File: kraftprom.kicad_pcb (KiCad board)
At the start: 2 copper layers, 67.5 x 82.6 mm, 21 parts, among them J1 Jumper_3_Bridged12, J2 PROGRAM, U1 PIC16F628A, U2 74HC164, U3 74HC164, U4 74HC164, U5 74LS245, U6 74LS165, U7 FTDI USB ADAPTER

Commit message: More PCB design.
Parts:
- moved G*** 0.91 mm to (141.7, 60.2)
- moved J1 0.20 mm to (139.6, 78.5)
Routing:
- net Earth: track 349.0 -> 330.6 mm, vias 8 -> 6
- net Net-(U1-RB2/TX/CK): track 64.9 -> 50.9 mm, vias 3 -> 1
- net Net-(U5-B2): track 62.3 -> 49.6 mm, vias 3 -> 1
- net Net-(U3-Q0): track 51.1 -> 43.3 mm, vias 3 -> 1
- net Net-(U1-RA3/AN3/CMP1): track 49.1 -> 42.0 mm, vias 1 -> 0
- net Net-(U3-Q7): track 51.4 -> 44.4 mm
- net Net-(U2-Q1): track 51.3 -> 44.7 mm
- net Net-(U1-RB1/RX/DT): track 63.9 -> 58.3 mm, vias 3 -> 0
- net Net-(J1-C): track 40.1 -> 34.9 mm
- net Net-(U2-Q5): track 73.2 -> 68.2 mm
- net Net-(U2-Q7): track 53.6 -> 48.6 mm, vias 3 -> 2
- net Net-(U2-Q2): track 46.6 -> 41.8 mm
- net Net-(U2-Q0): track 52.9 -> 48.5 mm
- net Net-(U2-Q6): track 32.0 -> 28.6 mm, vias 3 -> 2
- net Net-(U4-Q0): track 23.6 -> 20.4 mm, vias 2 -> 1
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
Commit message: More PCB design.
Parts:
- moved C6 1.91 mm to (100.4, 112.2)
- moved U6 1.77 mm to (92.8, 115.6)
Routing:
- net Earth: track 330.6 -> 327.8 mm, vias 6 -> 8
- net Net-(U5-B1): track 63.3 -> 61.0 mm
- net +5V: track 222.7 -> 220.8 mm, vias 1 -> 0
- net /~{VERLOAD}: track 21.3 -> 19.5 mm
- net Net-(U5-B0): track 55.3 -> 57.0 mm
- net Net-(U5-B7): track 75.5 -> 77.2 mm
- net /VERREAD: track 54.8 -> 53.2 mm
- net Net-(U5-B4): track 60.9 -> 62.3 mm
- net /VERCLK: track 16.5 -> 15.2 mm
- net Net-(U5-B6): track 71.8 -> 73.1 mm
- net Net-(U5-B5): track 65.9 -> 67.1 mm
- net Net-(U5-B3): track 58.0 -> 57.1 mm
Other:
- board size 67.5 x 82.6 mm -> 67.5 x 85.8 mm
- board text added: "Rev 1.0 ©2025 ARMCoder"
- board text removed: "Rev 1.0 ARMCoder"

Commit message: More PCB design (fixes).
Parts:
- moved J1 5.19 mm to (144.4, 80.3), turned to -90 degrees
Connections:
- U7 pad 12: Net-(U1-RA3/AN3/CMP1) -> unconnected-(U7-~{RTS}-Pad12)
- U7 pad 4: unconnected-(U7-~{CTS}-Pad4) -> Net-(U1-RA3/AN3/CMP1)
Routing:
- net Net-(U1-RA3/AN3/CMP1): track 42.0 -> 29.6 mm, vias 0 -> 1
- net /~{WE}: track 99.7 -> 94.6 mm
- net Net-(J1-B): track 39.2 -> 42.5 mm

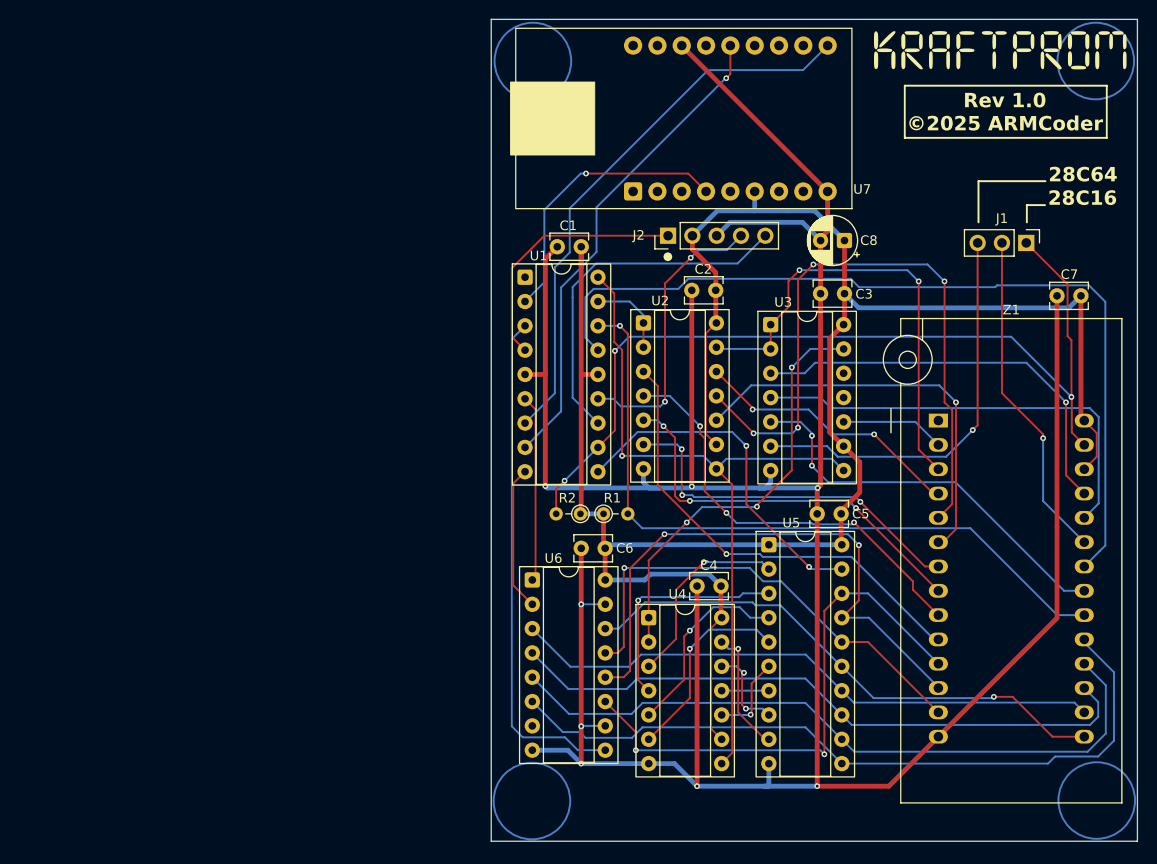
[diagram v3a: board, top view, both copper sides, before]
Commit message: More PCB design (clearances).
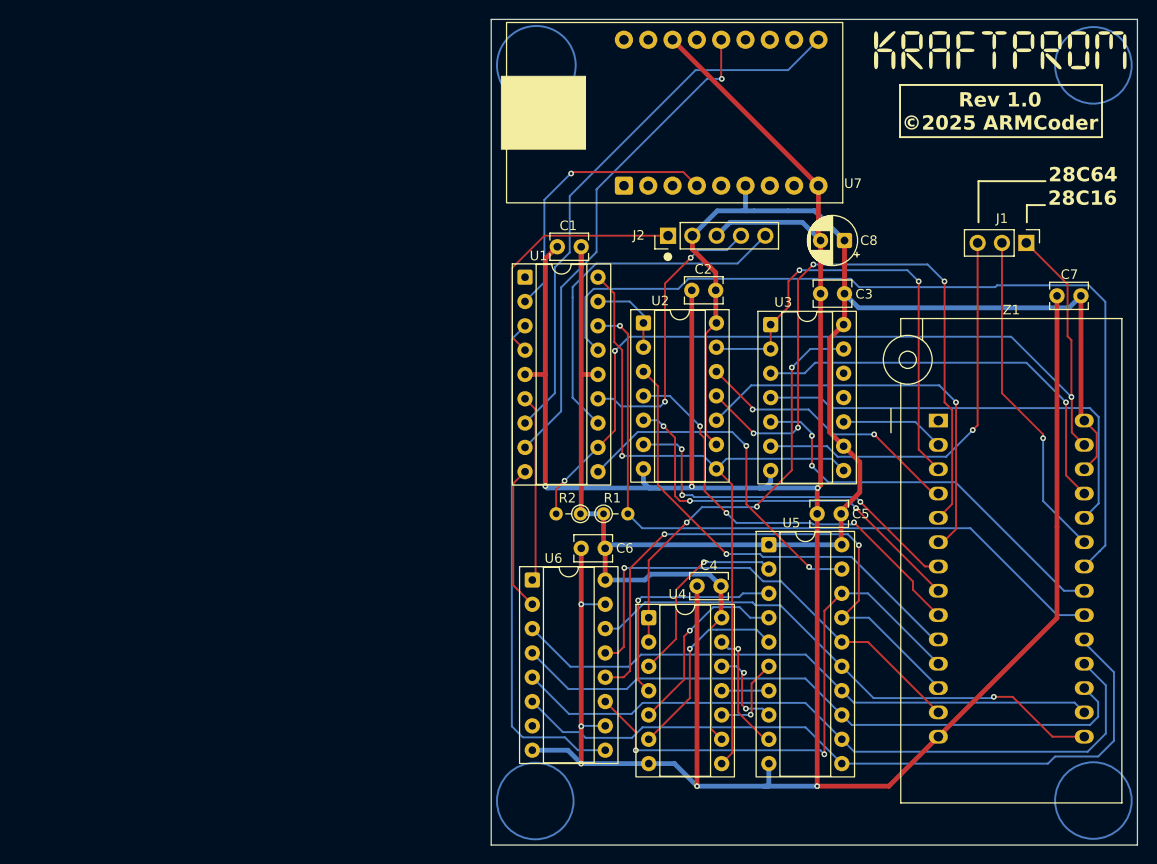
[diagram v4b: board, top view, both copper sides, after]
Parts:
- moved U7 1.13 mm to (104.9, 66.8)
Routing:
- net Net-(U1-RB2/TX/CK): track 50.9 -> 52.0 mm
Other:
- board size 67.5 x 85.8 mm -> 67.5 x 86.2 mm
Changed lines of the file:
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@@
 	(footprint "Kraft80:FTDI-ADAPTER"
 		(layer "F.Cu")
-		(at 105.86 67.355 180)
+		(at 104.9 66.75 180)
 		(property "Reference" "U7"
 			(at -21.39 -7.395 0)
@@
 	)
 	(gr_circle
-		(center 92.85 61.35)
-		(end 96.85 61.35)
+		(center 93.211265 61.8)
+		(end 97.211265 60.85)
 		(stroke
 			(width 0.2)
@@
 	)
 	(gr_circle
-		(center 151.75 138.6)
-		(end 155.75 138.6)
+		(center 151.4 138.6)
+		(end 155.4 138.6)
 		(stroke
 			(width 0.2)
@@
 	)
 	(gr_circle
-		(center 151.65 61.35)
-		(end 155.65 61.35)
+		(center 151.4 61.8)
+		(end 155.4 61.8)
 		(stroke
 			(width 0.2)
@@
 	)
 	(gr_circle
-		(center 92.75 138.65)
-		(end 96.75 138.65)
+		(center 93.1 138.65)
+		(end 97.1 138.65)
 		(stroke
 			(width 0.2)
@@
 	)
 	(gr_rect
-		(start 131.7 63.925)
-		(end 152.8 69.375)
+		(start 131.2 63.85)
+		(end 152.3 69.3)
 		(stroke
 			(width 0.2)
@@
 	(gr_rect
 		(start 88.5 57)
-		(end 156 142.85)
+		(end 156 143.25)
 		(stroke
 			(width 0.05)
@@
 	)
 	(gr_text "Rev 1.0\n©2025 ARMCoder"
-		(at 142.15 68.775 0)
+		(at 141.65 68.7 0)
 		(layer "F.SilkS")
 		(effects
@@
 	)
 	(segment
+		(start 122.68 79.63)
+		(end 122.68 74.37)
+		(width 0.5)
+		(layer "F.Cu")
+		(net 3)
+	)
+	(segment
+		(start 122.9 80.1)
+		(end 122.9 79.85)
+		(width 0.5)
+		(layer "F.Cu")
+		(net 3)
+	)
+	(segment
 		(start 147.6 119.5375)
 		(end 135.2075 131.93)
@@
 	)
 	(segment
-		(start 122.9 80.1)
-		(end 122.9 79.85)
-		(width 0.5)
-		(layer "F.Cu")
-		(net 3)
-	)
-	(segment
 		(start 147.6 110)
 		(end 147.6 119.5375)
@@
 	)
 	(segment
-		(start 123.64 79.11)
-		(end 123.64 74.975)
-		(width 0.5)
-		(layer "F.Cu")
-		(net 3)
-	)
-	(segment
 		(start 122.55 106)
 		(end 122.6 105.95)
@@
 	)
 	(segment
-		(start 123.625 74.975)
-		(end 123.64 74.975)
-		(width 0.5)
-		(layer "F.Cu")
-		(net 3)
-	)
-	(segment
-		(start 108.4 59.75)
-		(end 123.625 74.975)
+		(start 122.68 74.37)
+		(end 107.44 59.13)
 		(width 0.5)
 		(layer "F.Cu")
@@
 	)
 	(segment
-		(start 122.9 79.85)
-		(end 123.64 79.11)
-		(width 0.5)
-		(layer "F.Cu")
-		(net 3)
-	)
-	(segment
 		(start 97.95 130.8)
 		(end 97.9 130.85)
@@
 	)
 	(segment
-		(start 108.4 59.735)
-		(end 108.4 59.75)
-		(width 0.5)
-		(layer "F.Cu")
-		(net 3)
-	)
-	(segment
 		(start 109.45 85.3)
 		(end 109.45 105.8)
@@
 	)
 	(segment
+		(start 122.9 79.85)
+		(end 122.68 79.63)
+		(width 0.5)
+		(layer "F.Cu")
+		(net 3)
+	)
+	(segment
 		(start 97.9 118.1)
 		(end 97.9 130.85)
@@
 	)
 	(segment
-		(start 116.02 74.975)
-		(end 116.02 76.93)
-		(width 0.5)
-		(layer "B.Cu")
-		(net 21)
-	)
-	(segment
 		(start 117.5 111.88)
 		(end 100.77 111.88)
@@
 	(segment
 		(start 114.75 77)
-		(end 115.95 77)
-		(width 0.5)
-		(layer "B.Cu")
-		(net 21)
-	)
-	(segment
-		(start 116.35 75.305)
-		(end 116.02 74.975)
+		(end 115.1 77)
 		(width 0.5)
 		(layer "B.Cu")
@@
 	)
 	(segment
-		(start 116.02 76.93)
+		(start 115.1 77)
 		(end 115.95 77)
 		(width 0.5)
@@
 	)
 	(segment
+		(start 115.1 77)
+		(end 115.06 76.96)
+		(width 0.5)
+		(layer "B.Cu")
+		(net 21)
+	)
+	(segment
 		(start 150.1 85.88)
 		(end 148.849 87.131)
@@
 	)
 	(segment
+		(start 115.06 76.96)
+		(end 115.06 74.37)
+		(width 0.5)
+		(layer "B.Cu")
+		(net 21)
+	)
+	(segment
 		(start 100.77 111.88)
 		(end 100.4 112.25)
@@
 	)
 	(segment
-		(start 92.03 99.17)
-		(end 95.15 96.05)
+		(start 109.85 62.3)
+		(end 96.7 75.45)
 		(width 0.2)
 		(layer "B.Cu")
@@
 	(segment
 		(start 95.15 96.05)
-		(end 95.15 82.9)
+		(end 92.03 99.17)
 		(width 0.2)
 		(layer "B.Cu")
@@
 	)
 	(segment
-		(start 96.7 76.74358)
-		(end 111.14358 62.3)
+		(start 96.7 81.35)
+		(end 95.15 82.9)
 		(width 0.2)
 		(layer "B.Cu")
@@
 	)
 	(segment
-		(start 121.075 62.3)
-		(end 123.64 59.735)
+		(start 122.68 59.13)
+		(end 119.51 62.3)
 		(width 0.2)
 		(layer "B.Cu")
@@
 	)
 	(segment
-		(start 111.14358 62.3)
-		(end 121.075 62.3)
+		(start 95.15 82.9)
+		(end 95.15 96.05)
 		(width 0.2)
 		(layer "B.Cu")
@@
 	)
 	(segment
-		(start 95.15 82.9)
-		(end 96.7 81.35)
+		(start 119.51 62.3)
+		(end 109.85 62.3)
 		(width 0.2)
 		(layer "B.Cu")
@@
 	)
 	(segment
-		(start 96.7 81.35)
-		(end 96.7 76.74358)
+		(start 96.7 75.45)
+		(end 96.7 81.35)
 		(width 0.2)
 		(layer "B.Cu")
@@
 	)
 	(segment
-		(start 113.05 63.15)
-		(end 113.48 62.72)
+		(start 112.585331 63.214669)
+		(end 112.52 63.149338)
 		(width 0.2)
 		(layer "F.Cu")
@@
 	)
 	(segment
-		(start 113.48 62.72)
-		(end 113.48 59.735)
+		(start 112.52 63.149338)
+		(end 112.52 59.13)
 		(width 0.2)
 		(layer "F.Cu")
@@
 	)
 	(via
-		(at 113.05 63.15)
+		(at 112.585331 63.214669)
 		(size 0.6)
 		(drill 0.3)
@@
 	)
 	(segment
-		(start 113.05 63.15)
-		(end 112.98171 63.15)
+		(start 95.8 97.94)
+		(end 92.03 101.71)
 		(width 0.2)
 		(layer "B.Cu")
@@
 	)
 	(segment
-		(start 99.5 81.3)
-		(end 95.8 85)
+		(start 99.5 74.75)
+		(end 99.5 81.3)
 		(width 0.2)
 		(layer "B.Cu")
@@
 	)
 	(segment
-		(start 95.8 97.94)
-		(end 92.03 101.71)
+		(start 95.8 85)
+		(end 95.8 97.94)
 		(width 0.2)
 		(layer "B.Cu")
@@
 	)
 	(segment
-		(start 112.98171 63.15)
-		(end 99.5 76.63171)
+		(start 99.5 81.3)
+		(end 95.8 85)
 		(width 0.2)
 		(layer "B.Cu")
@@
 	)
 	(segment
-		(start 99.5 76.63171)
-		(end 99.5 81.3)
+		(start 99.5 74.75)
+		(end 111.035331 63.214669)
 		(width 0.2)
 		(layer "B.Cu")
@@
 	)
 	(segment
-		(start 95.8 85)
-		(end 95.8 97.94)
+		(start 111.035331 63.214669)
+		(end 112.585331 63.214669)
 		(width 0.2)
 		(layer "B.Cu")
@@
 	)
 	(segment
-		(start 109.065 73.1)
-		(end 110.94 74.975)
+		(start 97 72.95)
+		(end 108.56 72.95)
+		(width 0.2)
+		(layer "F.Cu")
+		(net 60)
+	)
+	(segment
+		(start 96.85 73.1)
+		(end 97 72.95)
 		(width 0.2)
 		(layer "F.Cu")
@@
 	)
 	(segment
-		(start 98.4 73.1)
-		(end 109.065 73.1)
+		(start 108.56 72.95)
+		(end 109.98 74.37)
 		(width 0.2)
 		(layer "F.Cu")
@@
 	)
 	(via
-		(at 98.4 73.1)
+		(at 96.85 73.1)
 		(size 0.6)
 		(drill 0.3)
@@
 	)
 	(segment
-		(start 94.05 76.9)
-		(end 97.85 73.1)
+		(start 94.05 84.45)
+		(end 92.03 86.47)
 		(width 0.2)
 		(layer "B.Cu")
@@
 	)
 	(segment
-		(start 97.85 73.1)
-		(end 98.4 73.1)
+		(start 96.8 73.1)
+		(end 94.05 75.85)
 		(width 0.2)
 		(layer "B.Cu")
@@
 	)
 	(segment
-		(start 92.03 86.47)
+		(start 94.05 75.85)
 		(end 94.05 84.45)
 		(width 0.2)
@@
 	)
 	(segment
-		(start 94.05 84.45)
-		(end 94.05 76.9)
+		(start 96.85 73.1)
+		(end 96.8 73.1)
 		(width 0.2)
 		(layer "B.Cu")

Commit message: More PCB fixes.
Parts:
- removed G***: LOGO, Kraft80:kraftprom
- C8: footprint Capacitor_THT:CP_Radial_D5.0mm_P2.50mm -> Capacitor_THT:CP_Radial_D6.3mm_P2.50mm
- R1, R2: footprint Resistor_THT:R_Axial_DIN0204_L3.6mm_D1.6mm_P2.54mm_Vertical -> Resistor_THT:R_Axial_DIN0207_L6.3mm_D2.5mm_P2.54mm_Vertical
- U1: footprint Package_DIP:DIP-18_W7.62mm_Socket -> Package_DIP:DIP-18_W7.62mm
- U2, U3, U4: footprint Package_DIP:DIP-14_W7.62mm_Socket -> Package_DIP:DIP-14_W7.62mm
- U5: footprint Package_DIP:DIP-20_W7.62mm_Socket -> Package_DIP:DIP-20_W7.62mm
- U6: footprint Package_DIP:DIP-16_W7.62mm_Socket -> Package_DIP:DIP-16_W7.62mm
- U7: footprint Kraft80:FTDI-ADAPTER -> KraftPROM:FTDI-ADAPTER
- Z1: footprint Socket:DIP_Socket-28_W11.9mm_W12.7mm_W15.24mm_W17.78mm_W18.5mm_3M_228-1277-00-0602J -> Socket:DIP_Socket-28_W11.9_W12.7_W15.24_W17.78_W18.5_3M_228-1277-00-0602J
- moved C8 82.0 mm to (49.5, 111.1), turned to -90 degrees
- moved J2 58.8 mm to (55.8, 108.5), turned to 0 degrees
- moved U7 55.4 mm to (50.3, 76.1), turned to 90 degrees
- moved U4 54.1 mm to (89.5, 67.7)
- moved C4 54.0 mm to (97.1, 64.5)
- moved C7 49.7 mm to (100.6, 81.8), turned to -90 degrees
- moved U2 46.7 mm to (62.8, 67.5)
- moved C3 46.7 mm to (83.9, 64.3)
- moved U3 46.6 mm to (76.3, 67.5)
- moved C2 46.5 mm to (70.5, 64.3)
- moved U5 43.9 mm to (76.4, 96.4)
- moved C5 43.9 mm to (84.0, 93.2)
- moved R1 37.1 mm to (69.8, 87.3), turned to 180 degrees
- moved J1 37.0 mm to (110.3, 66.0), turned to 90 degrees
- moved Z1 33.5 mm to (107.2, 80.5)
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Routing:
- net +5V: track 220.9 -> 271.9 mm
- net Net-(U4-Q7): track 13.0 -> 63.4 mm
- net Net-(U4-Q6): track 9.28 -> 59.0 mm, vias 2 -> 1
- net Net-(U4-Q5): track 4.93 -> 54.4 mm, vias 0 -> 1
- net Net-(U2-Q2): track 41.8 -> 84.9 mm, vias 3 -> 1
- net Net-(U4-Q4): track 9.26 -> 49.6 mm
- net Net-(U3-Q7): track 44.4 -> 8.14 mm, vias 3 -> 0
- net /PGDAT: track 8.69 -> 39.4 mm, vias 0 -> 1
- net Net-(U1-RB1/RX/DT): track 58.4 -> 30.7 mm
- net /PGCLK: track 76.3 -> 49.5 mm, vias 1 -> 3
- net Net-(U5-B6): track 73.1 -> 46.5 mm
- net Net-(U5-B7): track 77.2 -> 51.5 mm
- net /VERCLK: track 15.2 -> 40.7 mm, vias 0 -> 1
- net Net-(U5-B1): track 61.0 -> 35.6 mm
- net Net-(U2-Q6): track 28.6 -> 51.8 mm, vias 2 -> 1
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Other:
- board size 67.5 x 86.2 mm -> 87.6 x 62.2 mm
- board text added: "KRAFTPROM REV 1.0 © 2025 ARMCODER"
- board text removed: "Rev 1.0 ©2025 ARMCoder"
